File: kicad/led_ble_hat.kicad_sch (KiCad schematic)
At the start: 74 parts, among them J1 USB_C_Receptacle_USB2.0_14P, J2 Prog, J3 Battery, J4 DEBUG, J5 Strip, Q1 2N7002, Q2 AO3401A, Q3 2N7002, Q4 2N7002, Q5 BSS84, Q6 BSS84, U1 BQ24075RGT, U2 XC6206P332MR, U3 STM32WB55CGUx, Y1 32Mhz

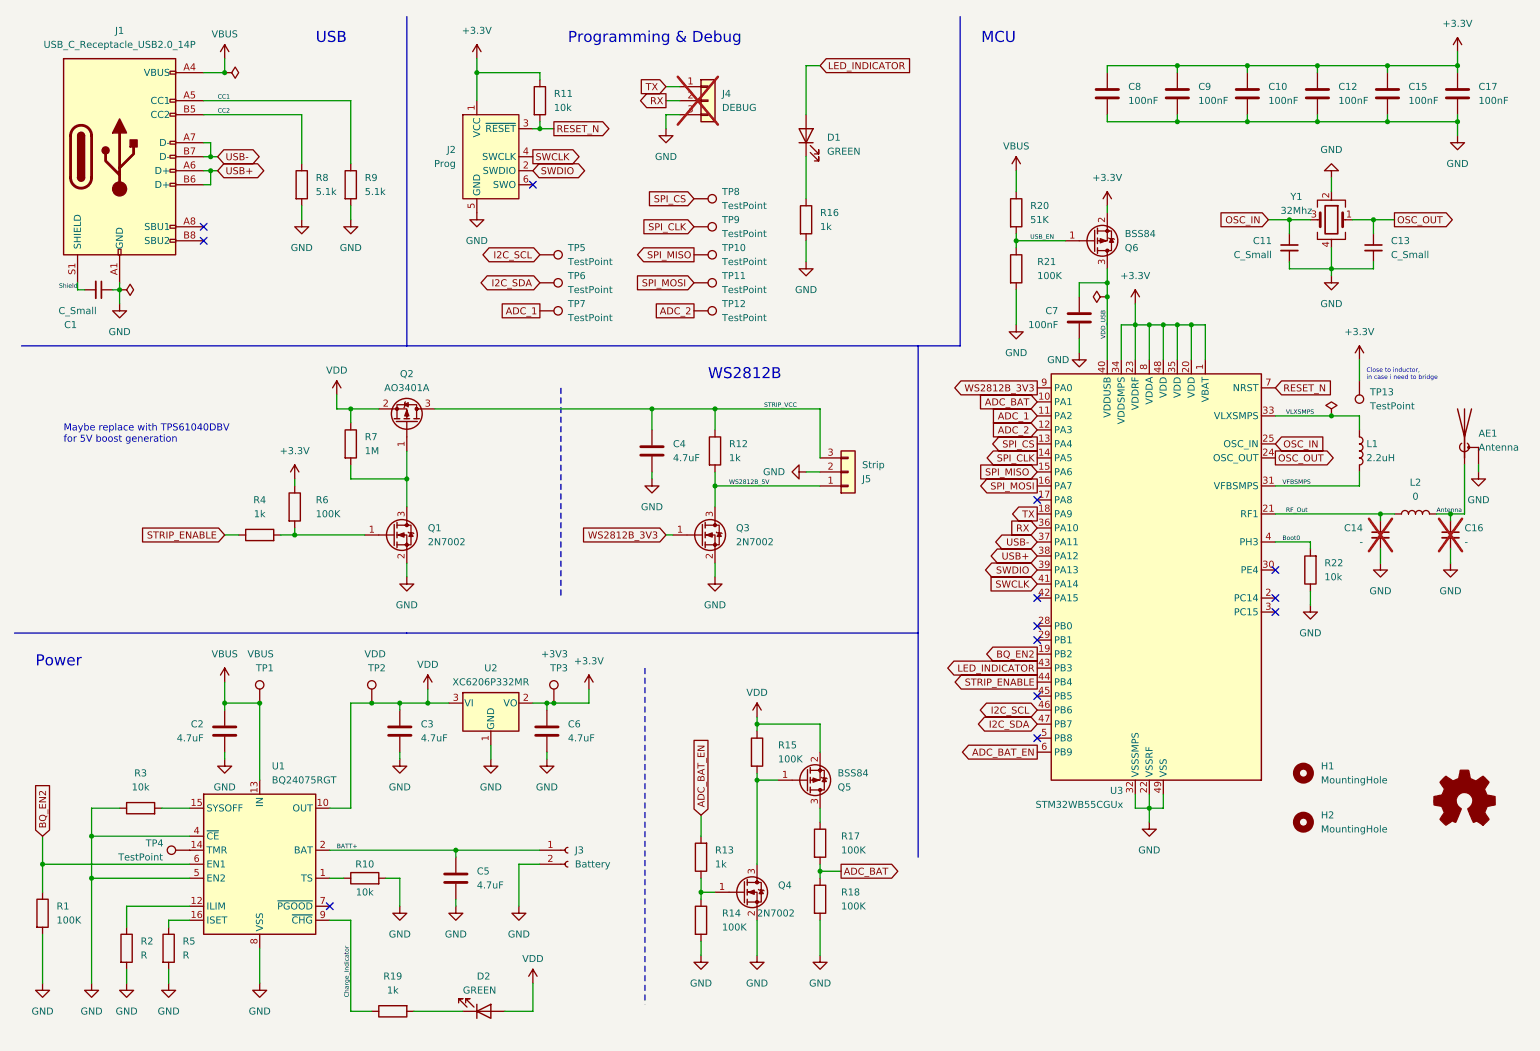
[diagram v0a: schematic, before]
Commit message: Replace battery charging ic, rough pcb placement
Replaced the battery charging ic with something much simpler.

Did a rough placement of the component onto a pcb for fit
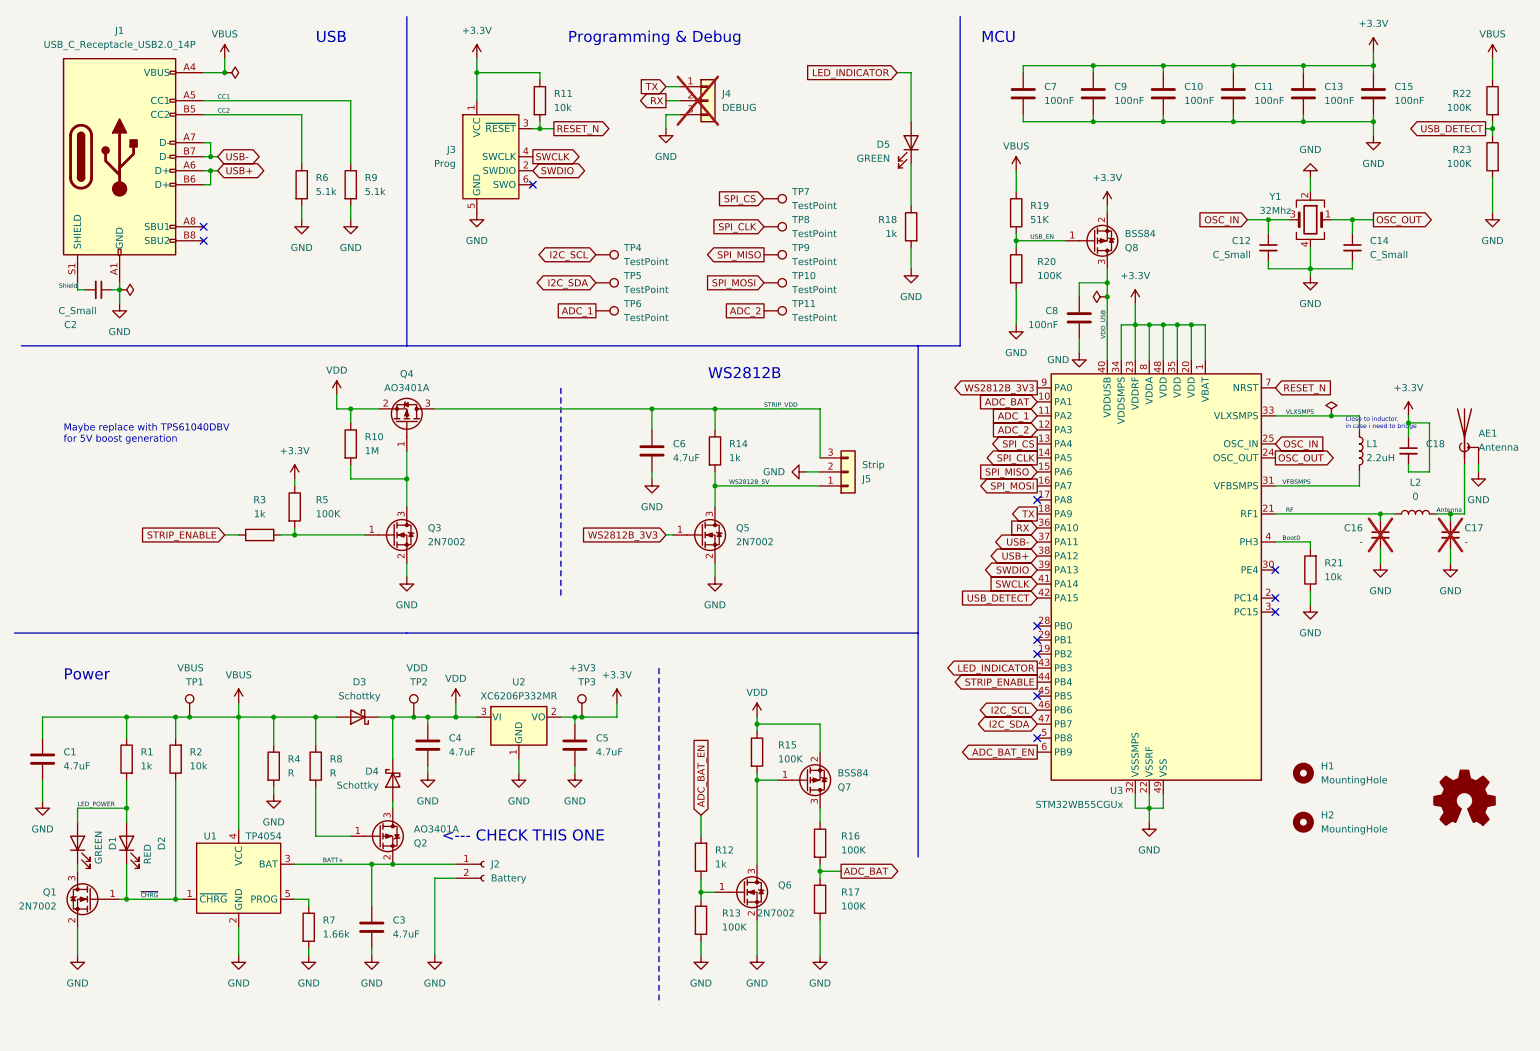
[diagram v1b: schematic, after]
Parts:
- removed R1: 100K, Resistor_SMD:R_0402_1005Metric, symbol Device:R
- removed R10, R3: 10k, Resistor_SMD:R_0402_1005Metric, symbol Device:R
- removed R5: R, Resistor_SMD:R_0402_1005Metric, symbol Device:R
- removed TP13, TP4: TestPoint, TestPoint:TestPoint_Pad_D1.0mm, symbol Connector:TestPoint
- removed U1: BQ24075RGT, Package_DFN_QFN:VQFN-16-1EP_3x3mm_P0.5mm_EP1.6x1.6mm, symbol Battery_Management:BQ24075RGT
- added C18: ~, Capacitor_SMD:C_0402_1005Metric, symbol Device:C_Small
- added D1: GREEN, LED_SMD:LED_0603_1608Metric, symbol Device:LED
- added D3, D4: Schottky, Diode_SMD:D_SOD-323, symbol Device:D_Schottky
- added Q1: 2N7002, Package_TO_SOT_SMD:SOT-23, symbol Transistor_FET:2N7002
- added Q2: AO3401A, Package_TO_SOT_SMD:SOT-23, symbol Transistor_FET:AO3401A
- added R22, R23: 100K, Resistor_SMD:R_0402_1005Metric, symbol Device:R
- added R4, R8: R, Resistor_SMD:R_0402_1005Metric, symbol Device:R
- added R7: 1.66k, Resistor_SMD:R_0402_1005Metric, symbol Device:R
- added U1: TP4054, Package_TO_SOT_SMD:SOT-23-5, symbol led-hat:TP4054-42
- D2: value GREEN -> RED; LCSC# C2986059 -> (none)
- R2: value R -> 10k; LCSC# (none) -> C25744
- renumbered C2 to C1, C12 to C11, C11 to C12, C15 to C13, C13 to C14, C17 to C15, C14 to C16, C16 to C17, C1 to C2, C5 to C3, C3 to C4, C6 to C5, C4 to C6, C8 to C7, C7 to C8, D1 to D5, J3 to J2, J2 to J3, Q1 to Q3, Q2 to Q4, Q3 to Q5, Q4 to Q6, Q5 to Q7, Q6 to Q8, R19 to R1, R7 to R10, R13 to R12, R14 to R13, R12 to R14, R17 to R16, R18 to R17, R16 to R18, R20 to R19, R21 to R20, R22 to R21, R4 to R3, R6 to R5, R8 to R6, TP11 to TP10, TP12 to TP11, TP5 to TP4, TP6 to TP5, TP7 to TP6, TP8 to TP7, TP9 to TP8, TP10 to TP9
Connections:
- net Charge_Indicator is gone; now on net VBUS: R1.1
- net +3.3V: now also C18.1, C18.2
- net BATT+: now also Q2.2 (S), U1.3 (BAT)
- net GND: now also Q1.2 (S), R23.2, R4.2, R7.2, U1.2 (GND); no longer R2.2
- net VBUS: now also R2.2, D3.2 (A), R22.1, R4.1, R8.1, U1.4 (VCC)
- net VDD: now also D3.1 (K), D4.1 (K); no longer D2.2 (A)
- net ~{CHRG}: now reaches R2.1
- net ~{CHRG}: now also D2.1 (K), Q1.1 (G), U1.1 (~{CHRG})
- net LED_POWER: now reaches R1.2
- net LED_POWER: now also D2.2 (A), D1.2 (A); no longer D2.1 (K)
- net USB_DETECT: now reaches U3.42 (PA15)
- net USB_DETECT: now also R22.2, R23.1
- net BQ_EN2: no longer names the net of U3.19 (PB2)
- net RF_Out renamed RF
- net STRIP_VCC renamed STRIP_VDD
- new net: D4.2 (A), Q2.3 (D)
- new net: Q2.1 (G), R8.2
- new net: D1.1 (K), Q1.3 (D)
- new net: R7.1, U1.5 (PROG)
- no-connect marks 13 -> 12
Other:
- note added: "<--- CHECK THIS ONE"
- moved on the sheet: C1, C10, C11, C12, C13, C14, C15, C3, C4, C5, C7, C9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

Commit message: Improved routing for PCB
Also added a vibration sensor on the backside of the PCB
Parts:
- removed C16: -, Capacitor_SMD:C_0402_1005Metric, symbol Device:C_Small
- removed D4: Schottky, Diode_SMD:D_SOD-323, symbol Device:D_Schottky
- removed R8: R, Resistor_SMD:R_0402_1005Metric, symbol Device:R
- removed TP11, TP4, TP5, TP6, TP7, TP8, TP9: TestPoint, TestPoint:TestPoint_Pad_D1.0mm, symbol Connector:TestPoint
- added F1: 2A, Fuse:Fuse_0603_1608Metric, symbol Device:Fuse
- added R24: 150R, Resistor_SMD:R_0402_1005Metric, symbol Device:R
- added R25, R26: 100k, Resistor_SMD:R_0402_1005Metric, symbol Device:R
- added SW1: SW_Reed, led-hat:SW-18010P, symbol Switch:SW_Reed
- C17, C18: LCSC# (none) -> -
- C2: value C_Small -> 100nF; LCSC# (none) -> C1525
- D2: LCSC# (none) -> C2286
- R10: value 1M -> 100k
- R13, R15, R16, R17, R20, R22, R23, R5: value 100K -> 100k
- R19: value 51K -> 51k
- R4: value R -> 100k; LCSC# (none) -> C25741
- R7: value 1.66k -> 1.5k; LCSC# (none) -> C25867
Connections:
- net ADC_2 is gone; now on net ADC_BAT: U3.12 (PA3)
- net SPI_CLK is gone; now on net LED_INDICATOR: U3.14 (PA5)
- net SPI_CS is gone; now on net STRIP_ENABLE: U3.13 (PA4)
- net +3.3V: now also R25.1; no longer R5.1
- net ADC_BAT: no longer U3.10 (PA1)
- net BATT+: now also Q2.3 (D), F1.1; no longer J2.1 (Pin_1), Q2.2 (S)
- net GND: now also R5.2, R24.2, SW1.1; no longer R7.2
- net LED_INDICATOR: no longer U3.43 (PB3)
- net STRIP_ENABLE: no longer U3.44 (PB4)
- net USB_DETECT: now also U3.44 (PB4); no longer U3.42 (PA15)
- net VBUS: now also Q2.1 (G)
- net VDD: now also Q2.2 (S)
- net at Q3.1 (G), R3.2: now also R5.1; no longer R5.2
- net POWER_VIBRATION: now reaches U3.28 (PB0)
- net POWER_VIBRATION: now also R26.1
- net VIBRATION: now reaches U3.29 (PB1)
- net VIBRATION: now also R25.2, R26.2, SW1.2
- net ADC_1: no longer names the net of U3.11 (PA2)
- net I2C_SCL: no longer names the net of U3.46 (PB6)
- net I2C_SDA: no longer names the net of U3.47 (PB7)
- net SPI_MISO: no longer names the net of U3.15 (PA6)
- new net: R24.1, R7.2
- new net: F1.2, J2.1 (Pin_1)
- no-connect marks 12 -> 17
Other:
- note added: "Set to 400mA"
- note added: "Wakeup-switch"
- note removed: "<--- CHECK THIS ONE"
- note removed: "Maybe replace with TPS61040DBV for 5V boost generation"
- moved on the sheet: C17, C4, D3, J2, L2, Q2, Q3, Q4, R10, R3, R4, R5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

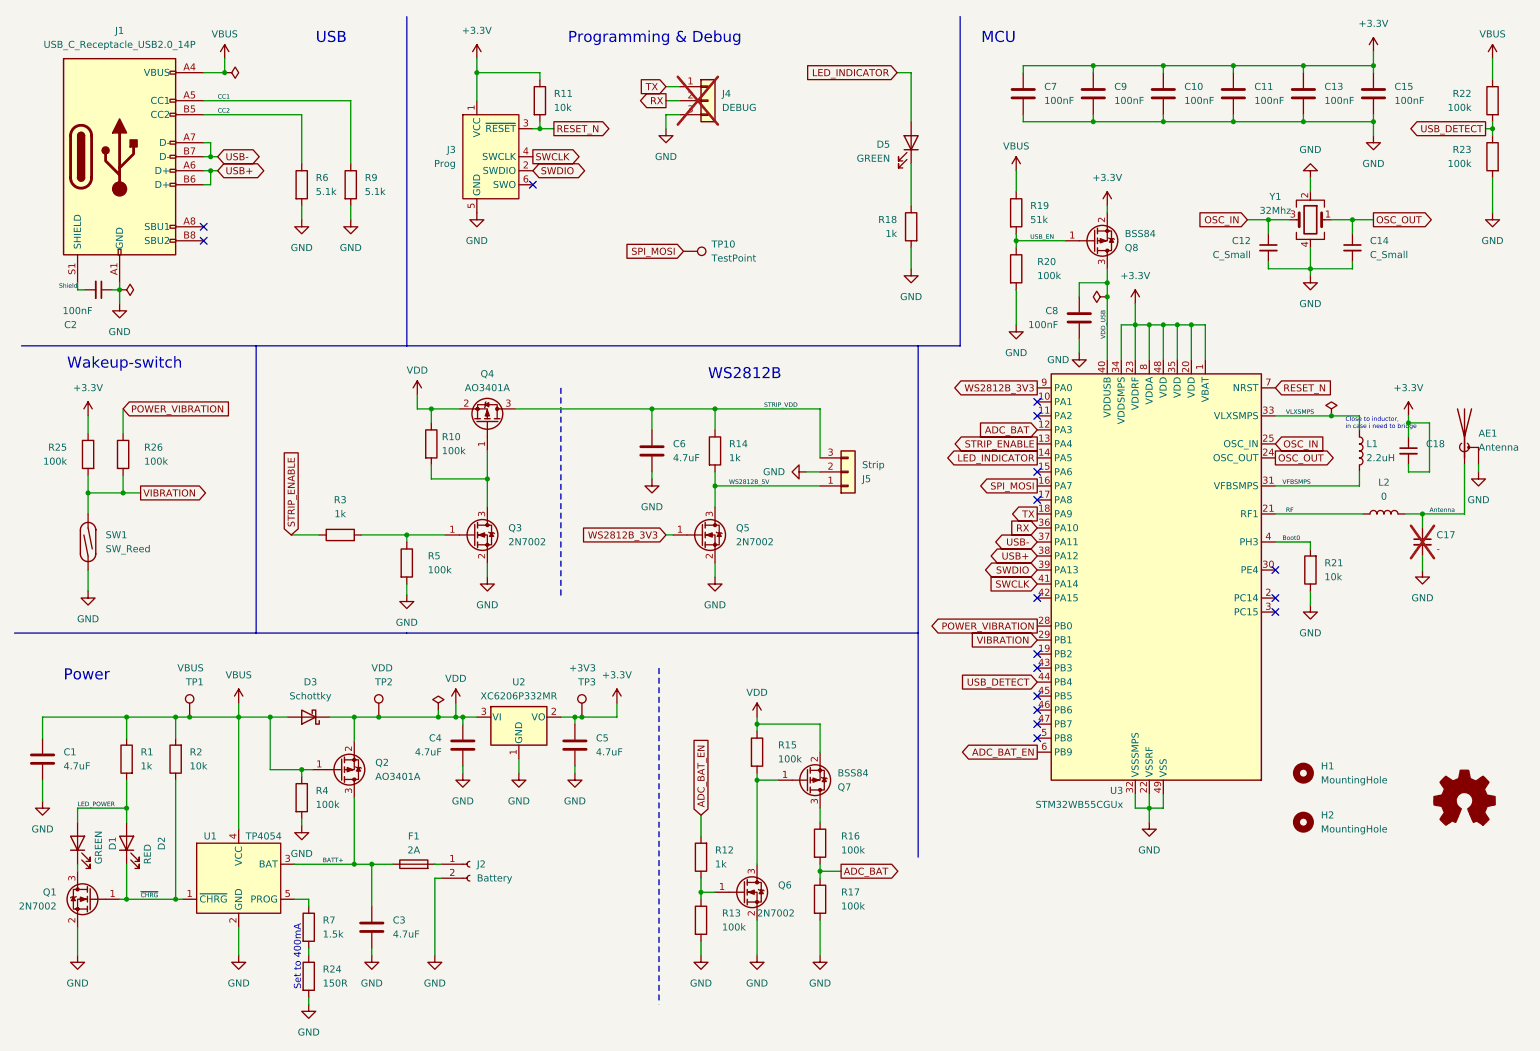
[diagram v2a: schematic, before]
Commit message: Add shake detector and final touches
PCB should be ready to order now.
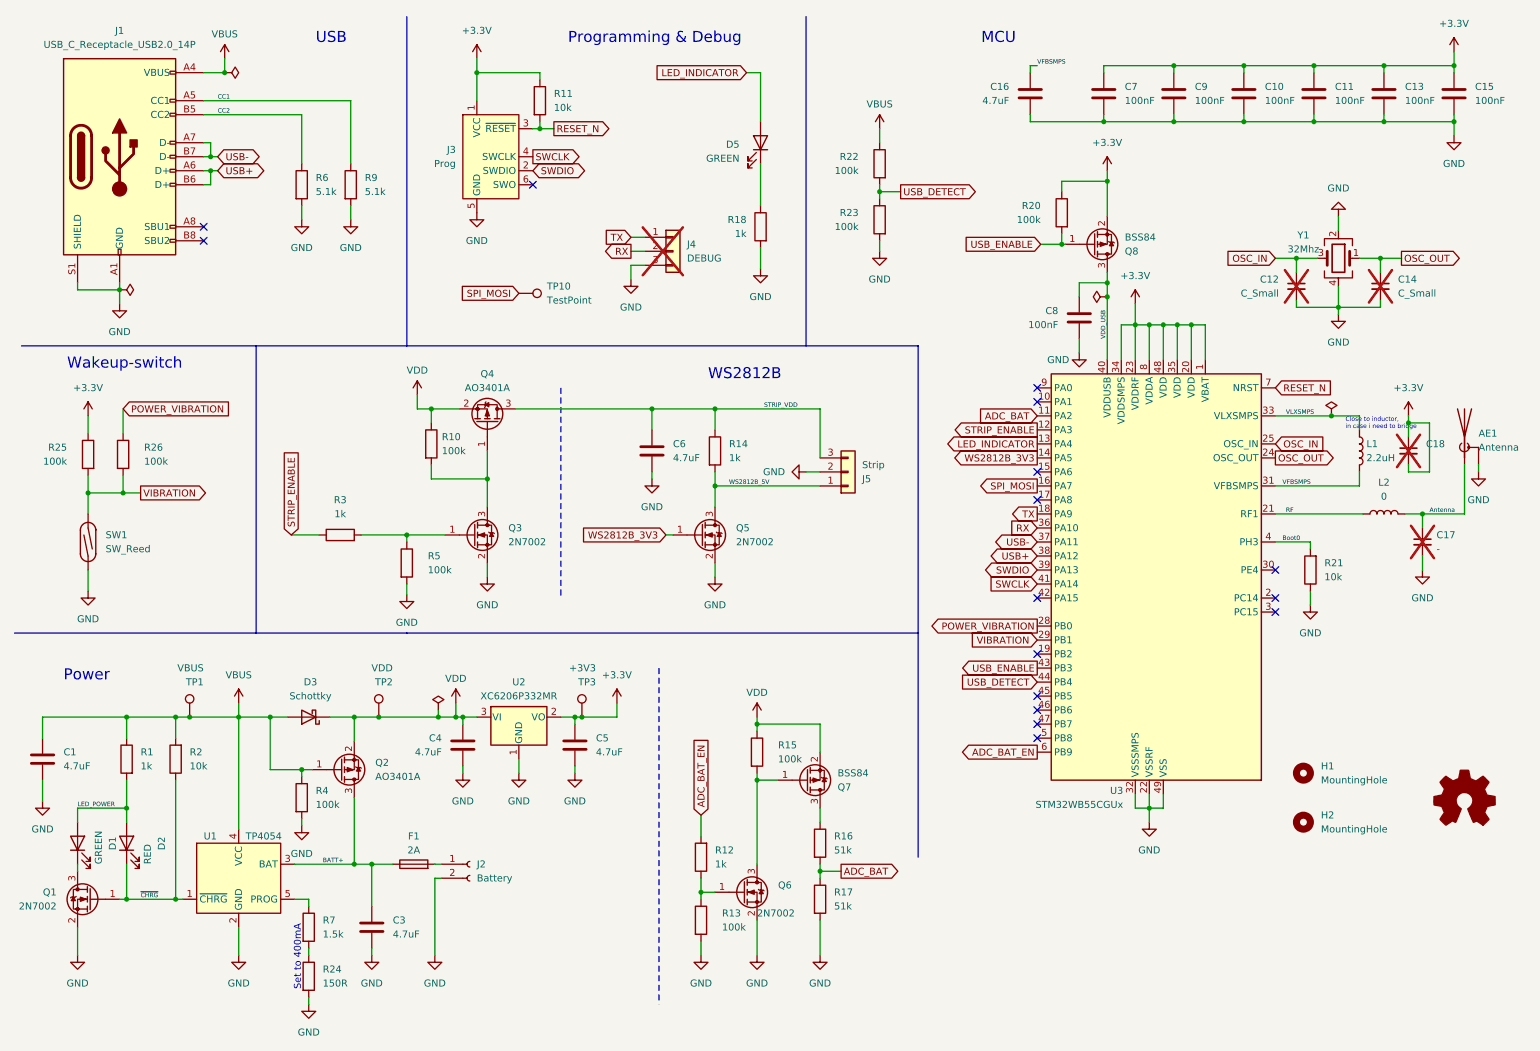
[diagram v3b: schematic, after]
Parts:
- removed C2: 100nF, Capacitor_SMD:C_0402_1005Metric, symbol Device:C_Small
- removed R19: 51k, Resistor_SMD:R_0402_1005Metric, symbol Device:R
- added C16: 4.7uF, Capacitor_SMD:C_0603_1608Metric, symbol Device:C
- C12, C14: LCSC# (none) -> -; now not fitted
- C18: now not fitted
- R10: footprint Resistor_SMD:R_0603_1608Metric -> Resistor_SMD:R_0402_1005Metric; LCSC# C22935 -> C25741
- R16, R17: value 100k -> 51k; LCSC# C25741 -> C25794
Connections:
- net Shield is gone; now on net GND: J1.S1 (SHIELD)
- net +3.3V: now also R20.1
- net ADC_BAT: now also U3.11 (PA2); no longer U3.12 (PA3)
- net GND: now also C16.2; no longer R20.2
- net LED_INDICATOR: now also U3.13 (PA4); no longer U3.14 (PA5)
- net STRIP_ENABLE: now also U3.12 (PA3); no longer U3.13 (PA4)
- net VFBSMPS: now also C16.1
- net WS2812B_3V3: now also U3.14 (PA5); no longer U3.9 (PA0)
- net USB_ENABLE: now reaches U3.43 (PB3)
- net USB_ENABLE: now also Q8.1 (G), R20.2
- removed net USB_EN: Q8.1 (G), R20.1
- no-connect marks 17 -> 16
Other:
- moved on the sheet: C10, C11, C13, C15, C7, C9, D5, J4, Q8, R18, R20, R22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

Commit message: Update to Kicad 8
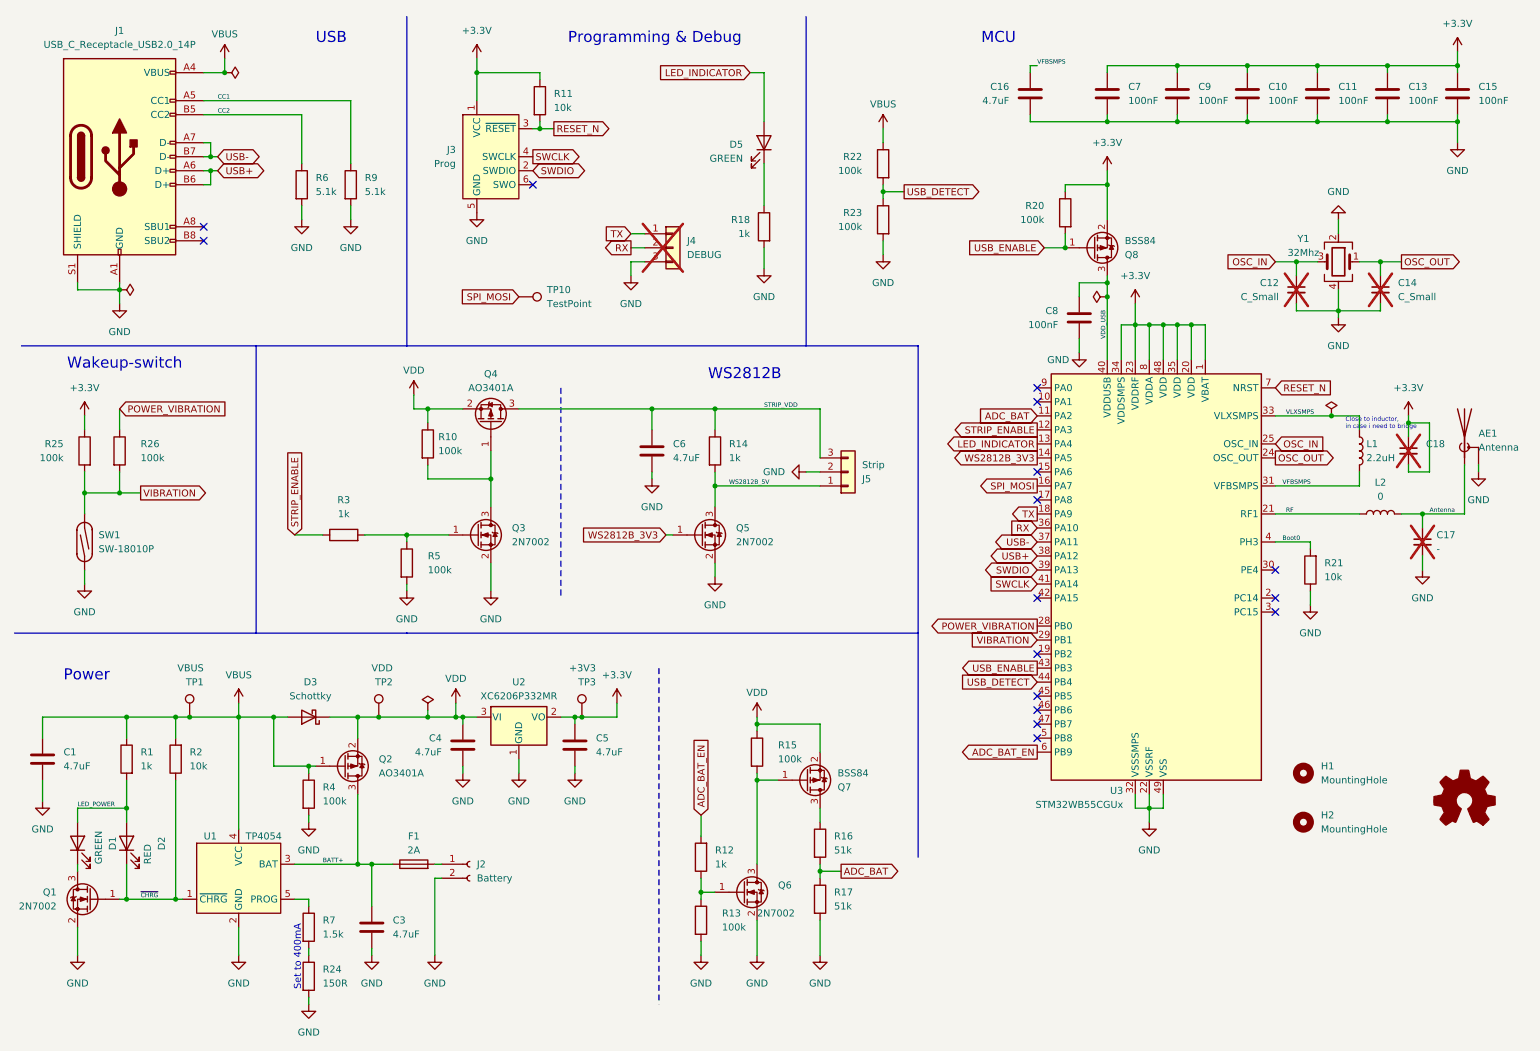
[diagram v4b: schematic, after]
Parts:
- SW1: value SW_Reed -> SW-18010P
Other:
- moved on the sheet: C10, C11, C12, C13, C14, C15, C7, C9, D5, J4, L2, Q2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
